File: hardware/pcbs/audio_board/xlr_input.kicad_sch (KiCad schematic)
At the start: 24 parts, among them J6 NC3FAH1, Q2 2N7002, Q3 SI2309CDS-T1-GE3

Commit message: fix mistakes in audioboard design
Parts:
- R22: value 100kΩ -> 100Ω; MPN R 100kΩ 125mW 1% 0805 -> R 100Ω 125mW 1% 0805
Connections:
- net +48V: now also Q3.2 (S); no longer Q3.3 (D)
- net GND: now also Q2.2 (S); no longer Q2.3 (D)
- net at R24.1: now also Q3.3 (D); no longer Q3.2 (S)
- net at R22.2: now also Q2.3 (D); no longer Q2.2 (S)
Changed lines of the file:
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@@
 		(lib_id "Transistor_FET:Si2371EDS")
 		(at 97.79 48.26 0)
+		(mirror x)
 		(unit 1)
 		(exclude_from_sim no)
@@
 		(dnp no)
 		(property "Reference" "Q3"
-			(at 104.14 46.9899 0)
+			(at 104.14 49.5301 0)
 			(effects
 				(font
@@
 		)
 		(property "Value" "SI2309CDS-T1-GE3"
-			(at 104.14 49.5299 0)
+			(at 104.14 46.9901 0)
 			(effects
 				(font
@@
 		)
 		(property "Footprint" "Package_TO_SOT_SMD:SOT-23"
-			(at 102.87 50.165 0)
+			(at 102.87 46.355 0)
 			(effects
 				(font
@@
 		)
 		(property "Datasheet" "http://www.vishay.com/docs/63924/si2371eds.pdf"
-			(at 102.87 52.07 0)
+			(at 102.87 44.45 0)
 			(effects
 				(font
@@
 			)
 		)
-		(property "Value" "100kΩ"
+		(property "Value" "100Ω"
 			(at 74.93 55.8799 0)
 			(effects
@@
 			)
 		)
-		(property "MPN" "R 100kΩ 125mW 1% 0805"
+		(property "MPN" "R 100Ω 125mW 1% 0805"
 			(at 72.39 54.61 0)
 			(effects
@@
 		(lib_id "Transistor_FET:2N7002")
 		(at 69.85 66.04 0)
-		(mirror x)
 		(unit 1)
 		(exclude_from_sim no)
@@
 		(dnp no)
 		(property "Reference" "Q2"
+			(at 74.93 67.31 0)
+			(effects
+				(font
+					(size 1.27 1.27)
+				)
+				(justify left)
+			)
+		)
+		(property "Value" "2N7002"
 			(at 74.93 64.77 0)
 			(effects
@@
 			)
 		)
-		(property "Value" "2N7002"
-			(at 74.93 67.31 0)
-			(effects
-				(font
-					(size 1.27 1.27)
-				)
-				(justify left)
-			)
-		)
 		(property "Footprint" "Package_TO_SOT_SMD:SOT-23"
-			(at 74.93 64.135 0)
+			(at 74.93 67.945 0)
 			(effects
 				(font
@@
 		)
 		(property "Datasheet" "https://www.onsemi.com/pub/Collateral/NDS7002A-D.PDF"
-			(at 74.93 62.23 0)
-			(effects
-				(font
+			(at 74.93 69.85 0)
+			(effects
+				(font

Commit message: final fixes on audio board
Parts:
- C39, C40: MPN C 1nF 100V 0805 -> C 1nF LowESR 100V 0805
- C42: MPN C 2.2nF 100V 0805 -> C 2.2nF LowESR 100V 0805
- C43, C44: MPN C 10μF 100V P2 -> C 10μF LowESR 100V P2
- renumbered R20 to R18, R21 to R19, R22 to R20, R23 to R21, R24 to R22, R25 to R23, R26 to R24, R27 to R25, R28 to R26, R29 to R27, R30 to R28, R31 to R29

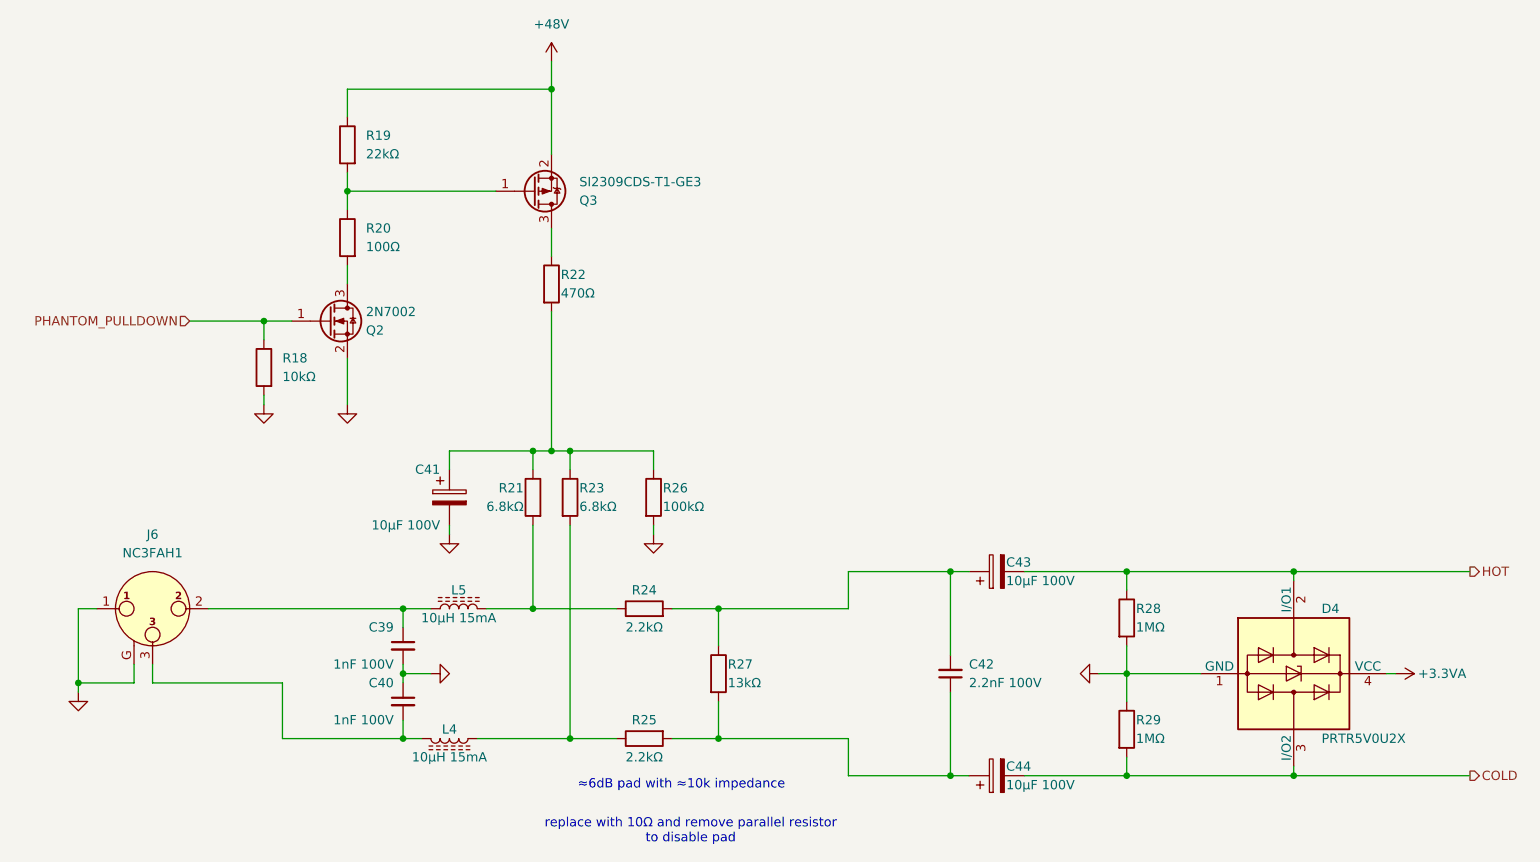
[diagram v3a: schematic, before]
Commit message: fix audioboard phantom power and some labels
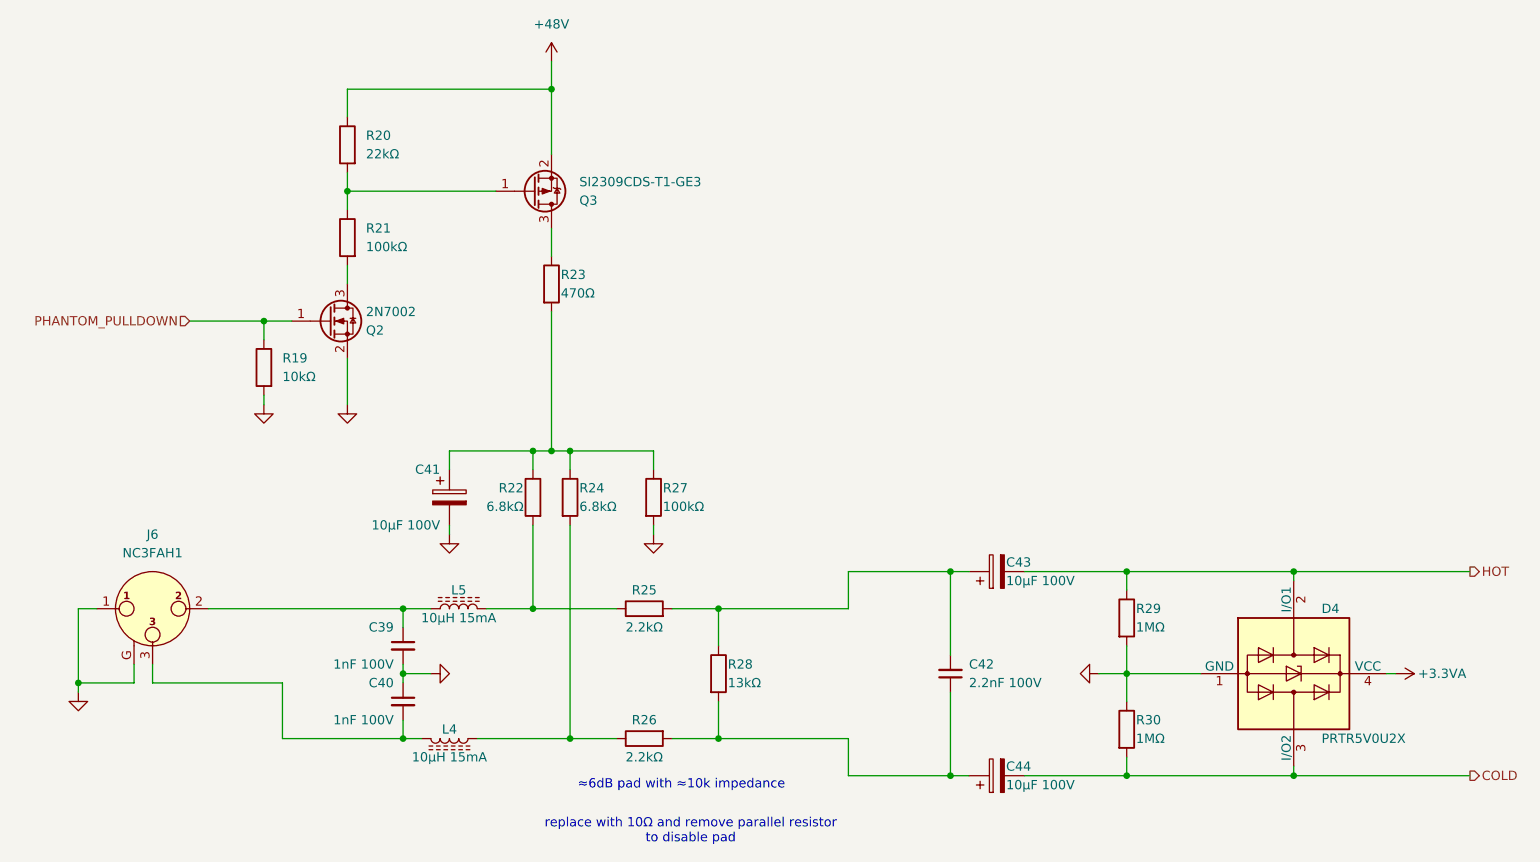
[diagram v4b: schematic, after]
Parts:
- R21: renamed from R20; value 100Ω -> 100kΩ; MPN R 100Ω 125mW 1% 0805 -> R 100kΩ 125mW 1% 0805
- renumbered R18 to R19, R19 to R20, R21 to R22, R22 to R23, R23 to R24, R24 to R25, R25 to R26, R26 to R27, R27 to R28, R28 to R29, R29 to R30
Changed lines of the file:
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@@
 		(length 2.54)
 		(shape round)
+		(at 85.09 48.26 0)
+		(fields_autoplaced yes)
+		(effects
+			(font
+				(size 1.27 1.27)
+			)
+			(justify left bottom)
+		)
+		(property "Netclass" "Phantom"
+			(at 85.7885 45.72 0)
+			(effects
+				(font
+					(size 1.27 1.27)
+				)
+				(justify left)
+			)
+		)
+		(property "Component Class" ""
+			(at -179.07 0 0)
+			(effects
+				(font
+					(size 1.27 1.27)
+					(italic yes)
+				)
+			)
+		)
+	)
+	(netclass_flag ""
+		(length 2.54)
+		(shape round)
+		(at 72.39 59.69 90)
+		(fields_autoplaced yes)
+		(effects
+			(font
+				(size 1.27 1.27)
+			)
+			(justify left bottom)
+		)
+		(property "Netclass" "Phantom"
+			(at 69.85 58.9915 90)
+			(effects
+				(font
+					(size 1.27 1.27)
+				)
+				(justify left)
+			)
+		)
+		(property "Component Class" ""
+			(at -191.77 11.43 0)
+			(effects
+				(font
+					(size 1.27 1.27)
+					(italic yes)
+				)
+			)
+		)
+	)
+	(netclass_flag ""
+		(length 2.54)
+		(shape round)
 		(at 128.27 105.41 0)
 		(fields_autoplaced yes)
@@
 		(on_board yes)
 		(dnp no)
-		(property "Reference" "R25"
+		(property "Reference" "R26"
 			(at 113.03 120.65 90)
 			(effects
@@
 			(project "audio_board"
 				(path "/54443f96-c7c5-4432-b890-45b14a1547a1/8957bb4e-7be5-4513-a482-a60a2150a7cb"
-					(reference "R49")
+					(reference "R50")
 					(unit 1)
 				)
 				(path "/54443f96-c7c5-4432-b890-45b14a1547a1/91e2e940-fc71-4db8-9476-c8ec62bf0617"
-					(reference "R37")
+					(reference "R38")
 					(unit 1)
 				)
 				(path "/54443f96-c7c5-4432-b890-45b14a1547a1/b0f2da11-13c7-4314-8470-ff6d99797a55"
-					(reference "R25")
+					(reference "R26")
 					(unit 1)
 				)
@@
 		(on_board yes)
 		(dnp no)
-		(property "Reference" "R24"
+		(property "Reference" "R25"
 			(at 113.03 102.87 90)
 			(effects
@@
 			(project "audio_board"
 				(path "/54443f96-c7c5-4432-b890-45b14a1547a1/8957bb4e-7be5-4513-a482-a60a2150a7cb"
-					(reference "R48")
+					(reference "R49")
 					(unit 1)
 				)
 				(path "/54443f96-c7c5-4432-b890-45b14a1547a1/91e2e940-fc71-4db8-9476-c8ec62bf0617"
-					(reference "R36")
+					(reference "R37")
 					(unit 1)
 				)
 				(path "/54443f96-c7c5-4432-b890-45b14a1547a1/b0f2da11-13c7-4314-8470-ff6d99797a55"
-					(reference "R24")
+					(reference "R25")
 					(unit 1)
 				)
@@
 		(on_board yes)
 		(dnp no)
-		(property "Reference" "R23"
+		(property "Reference" "R24"
 			(at 104.14 88.9 0)
 			(effects
@@
 			(project "audio_board"
 				(path "/54443f96-c7c5-4432-b890-45b14a1547a1/8957bb4e-7be5-4513-a482-a60a2150a7cb"
-					(reference "R47")
+					(reference "R48")
 					(unit 1)
 				)
 				(path "/54443f96-c7c5-4432-b890-45b14a1547a1/91e2e940-fc71-4db8-9476-c8ec62bf0617"
-					(reference "R35")
+					(reference "R36")
 					(unit 1)
 				)
 				(path "/54443f96-c7c5-4432-b890-45b14a1547a1/b0f2da11-13c7-4314-8470-ff6d99797a55"
-					(reference "R23")
+					(reference "R24")
 					(unit 1)
 				)
@@
 		(on_board yes)
 		(dnp no)
-		(property "Reference" "R28"
+		(property "Reference" "R29"
 			(at 180.34 105.41 0)
 			(effects
@@
 			(project "audio_board"
 				(path "/54443f96-c7c5-4432-b890-45b14a1547a1/8957bb4e-7be5-4513-a482-a60a2150a7cb"
-					(reference "R52")
+					(reference "R53")
 					(unit 1)
 				)
 				(path "/54443f96-c7c5-4432-b890-45b14a1547a1/91e2e940-fc71-4db8-9476-c8ec62bf0617"
-					(reference "R40")
+					(reference "R41")
 					(unit 1)
 				)
 				(path "/54443f96-c7c5-4432-b890-45b14a1547a1/b0f2da11-13c7-4314-8470-ff6d99797a55"
-					(reference "R28")
+					(reference "R29")
 					(unit 1)
 				)
@@
 		(dnp no)
 		(fields_autoplaced yes)
-		(property "Reference" "R20"
+		(property "Reference" "R21"
 			(at 74.93 53.3399 0)
 			(effects
@@
 			)
 		)
-		(property "Value" "100Ω"
+		(property "Value" "100kΩ"
 			(at 74.93 55.8799 0)
 			(effects
@@
 			)
 		)
-		(property "MPN" "R 100Ω 125mW 1% 0805"
+		(property "MPN" "R 100kΩ 125mW 1% 0805"
 			(at 72.39 54.61 0)
 			(effects
@@
 			(project "audio_board"
 				(path "/54443f96-c7c5-4432-b890-45b14a1547a1/8957bb4e-7be5-4513-a482-a60a2150a7cb"
-					(reference "R44")
+					(reference "R45")
 					(unit 1)
 				)
 				(path "/54443f96-c7c5-4432-b890-45b14a1547a1/91e2e940-fc71-4db8-9476-c8ec62bf0617"
-					(reference "R32")
+					(reference "R33")
 					(unit 1)
 				)
 				(path "/54443f96-c7c5-4432-b890-45b14a1547a1/b0f2da11-13c7-4314-8470-ff6d99797a55"
-					(reference "R20")
+					(reference "R21")
 					(unit 1)
 				)
@@
 		(on_board yes)
 		(dnp no)
-		(property "Reference" "R21"
+		(property "Reference" "R22"
 			(at 96.52 88.9 0)
 			(effects
@@
 			(project "audio_board"
 				(path "/54443f96-c7c5-4432-b890-45b14a1547a1/8957bb4e-7be5-4513-a482-a60a2150a7cb"
-					(reference "R45")
+					(reference "R46")
 					(unit 1)
 				)
 				(path "/54443f96-c7c5-4432-b890-45b14a1547a1/91e2e940-fc71-4db8-9476-c8ec62bf0617"
-					(reference "R33")
+					(reference "R34")
 					(unit 1)
 				)
 				(path "/54443f96-c7c5-4432-b890-45b14a1547a1/b0f2da11-13c7-4314-8470-ff6d99797a55"
-					(reference "R21")
+					(reference "R22")
 					(unit 1)
 				)
@@
 		(on_board yes)
 		(dnp no)
-		(property "Reference" "R26"
+		(property "Reference" "R27"
 			(at 115.57 88.9 0)
 			(effects
@@
 			(project "audio_board"
 				(path "/54443f96-c7c5-4432-b890-45b14a1547a1/8957bb4e-7be5-4513-a482-a60a2150a7cb"
-					(reference "R50")
+					(reference "R51")
 					(unit 1)
 				)
 				(path "/54443f96-c7c5-4432-b890-45b14a1547a1/91e2e940-fc71-4db8-9476-c8ec62bf0617"
-					(reference "R38")
+					(reference "R39")
 					(unit 1)
 				)
 				(path "/54443f96-c7c5-4432-b890-45b14a1547a1/b0f2da11-13c7-4314-8470-ff6d99797a55"
-					(reference "R26")
+					(reference "R27")
 					(unit 1)
 				)
@@
 		(on_board yes)
 		(dnp no)
-		(property "Reference" "R29"
+		(property "Reference" "R30"
 			(at 180.34 120.65 0)
 			(effects
@@
 			(project "audio_board"
 				(path "/54443f96-c7c5-4432-b890-45b14a1547a1/8957bb4e-7be5-4513-a482-a60a2150a7cb"
-					(reference "R53")
+					(reference "R54")
 					(unit 1)
 				)
 				(path "/54443f96-c7c5-4432-b890-45b14a1547a1/91e2e940-fc71-4db8-9476-c8ec62bf0617"
-					(reference "R41")
+					(reference "R42")
 					(unit 1)
 				)
 				(path "/54443f96-c7c5-4432-b890-45b14a1547a1/b0f2da11-13c7-4314-8470-ff6d99797a55"
-					(reference "R29")
+					(reference "R30")
 					(unit 1)
 				)
@@
 		(dnp no)
 		(fields_autoplaced yes)
-		(property "Reference" "R19"
+		(property "Reference" "R20"
 			(at 74.93 40.6399 0)
 			(effects
@@
 			(project "audio_board"
 				(path "/54443f96-c7c5-4432-b890-45b14a1547a1/8957bb4e-7be5-4513-a482-a60a2150a7cb"
-					(reference "R43")
+					(reference "R44")
 					(unit 1)
 				)
 				(path "/54443f96-c7c5-4432-b890-45b14a1547a1/91e2e940-fc71-4db8-9476-c8ec62bf0617"
-					(reference "R31")
+					(reference "R32")
 					(unit 1)
 				)
 				(path "/54443f96-c7c5-4432-b890-45b14a1547a1/b0f2da11-13c7-4314-8470-ff6d99797a55"
-					(reference "R19")
+					(reference "R20")
 					(unit 1)
 				)
@@
 		(on_board yes)
 		(dnp no)
-		(property "Reference" "R22"
+		(property "Reference" "R23"
 			(at 101.6 59.69 0)
 			(effects
@@
 			(project "audio_board"
 				(path "/54443f96-c7c5-4432-b890-45b14a1547a1/8957bb4e-7be5-4513-a482-a60a2150a7cb"
-					(reference "R46")
+					(reference "R47")
 					(unit 1)
 				)
 				(path "/54443f96-c7c5-4432-b890-45b14a1547a1/91e2e940-fc71-4db8-9476-c8ec62bf0617"
-					(reference "R34")
+					(reference "R35")
 					(unit 1)
 				)
 				(path "/54443f96-c7c5-4432-b890-45b14a1547a1/b0f2da11-13c7-4314-8470-ff6d99797a55"
-					(reference "R22")
+					(reference "R23")
 					(unit 1)
 				)
@@
 		(on_board yes)
 		(dnp no)
-		(property "Reference" "R27"
+		(property "Reference" "R28"
 			(at 124.46 113.03 0)
 			(effects
@@
 			(project "audio_board"
 				(path "/54443f96-c7c5-4432-b890-45b14a1547a1/8957bb4e-7be5-4513-a482-a60a2150a7cb"
-					(reference "R51")
+					(reference "R52")
 					(unit 1)
 				)
 				(path "/54443f96-c7c5-4432-b890-45b14a1547a1/91e2e940-fc71-4db8-9476-c8ec62bf0617"
-					(reference "R39")
+					(reference "R40")
 					(unit 1)
 				)
 				(path "/54443f96-c7c5-4432-b890-45b14a1547a1/b0f2da11-13c7-4314-8470-ff6d99797a55"
-					(reference "R27")
+					(reference "R28")
 					(unit 1)
 				)
@@
 		(dnp no)
 		(fields_autoplaced yes)
-		(property "Reference" "R18"
+		(property "Reference" "R19"
 			(at 63.5 71.1199 0)
 			(effects
@@
 			(project "audio_board"
 				(path "/54443f96-c7c5-4432-b890-45b14a1547a1/8957bb4e-7be5-4513-a482-a60a2150a7cb"
-					(reference "R42")
+					(reference "R43")
 					(unit 1)
 				)
 				(path "/54443f96-c7c5-4432-b890-45b14a1547a1/91e2e940-fc71-4db8-9476-c8ec62bf0617"
-					(reference "R30")
+					(reference "R31")
 					(unit 1)
 				)
 				(path "/54443f96-c7c5-4432-b890-45b14a1547a1/b0f2da11-13c7-4314-8470-ff6d99797a55"
-					(reference "R18")
+					(reference "R19")
 					(unit 1)
 				)
